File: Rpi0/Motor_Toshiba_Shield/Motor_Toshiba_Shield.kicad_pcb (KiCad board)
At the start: 2 copper layers, 29.8 x 64.8 mm, 34 parts, among them J1 Screw_Terminal_01x02, J10 Conn_01x04_Female, J11 Conn_01x04_Female, J2 Conn_02x01, J3 Screw_Terminal_01x02, J4 Screw_Terminal_01x02, J5 Screw_Terminal_01x02, J6 Screw_Terminal_01x02, J7 Conn_02x01, J8 Conn_01x04_Female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

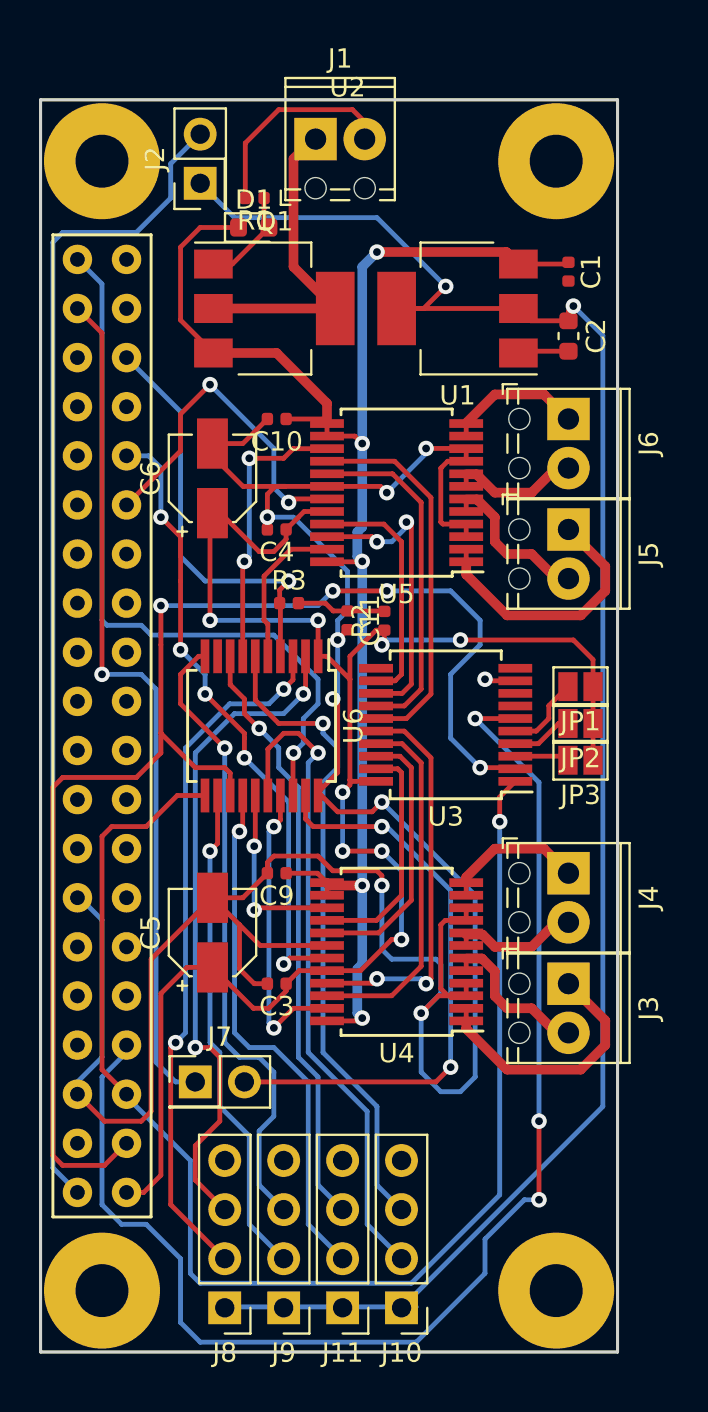
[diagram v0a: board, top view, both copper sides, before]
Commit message: Replaced pic16lf1509 and MCP by pic16f1777
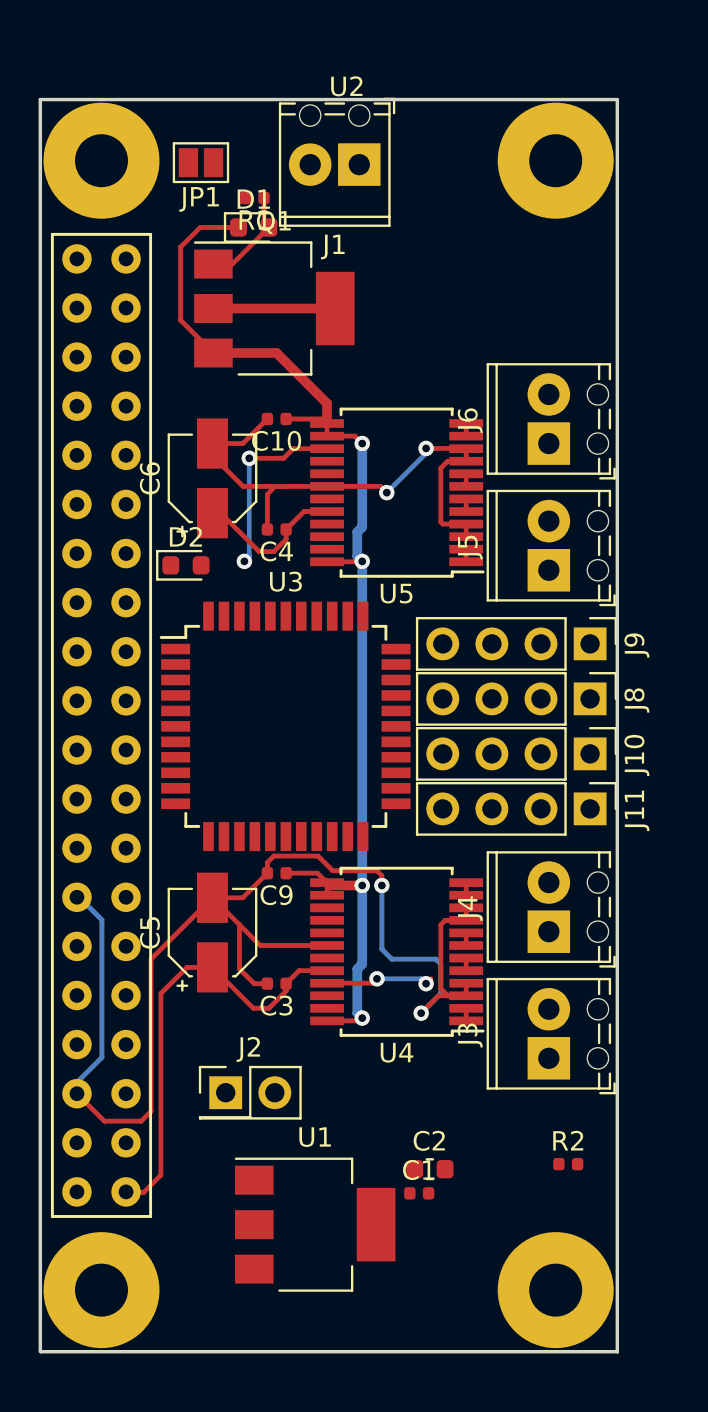
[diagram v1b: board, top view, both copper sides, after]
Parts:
- removed C11: 1uF, Capacitor_SMD:C_0402_1005Metric
- removed J7: Conn_02x01, Connector_PinHeader_2.54mm:PinHeader_2x01_P2.54mm_Vertical
- removed JP2, JP3: SolderJumper_2_Open, Jumper:SolderJumper-2_P1.3mm_Open_Pad1.0x1.5mm
- removed R3: 470, Resistor_SMD:R_0402_1005Metric
- removed U6: PIC16F1509-ISS, Package_SO:SSOP-20_5.3x7.2mm_P0.65mm
- added D2: LED, LED_SMD:LED_0603_1608Metric, F.Cu at (114.8, 86.3)
- R2: value 10k -> 50
- U3: value MCP23008_SSOP -> PIC16F1777-TQFP; footprint Package_SO:SSOP-20_5.3x7.2mm_P0.65mm -> Package_QFP:TQFP-44_10x10mm_P0.8mm
- moved C1 48.3 mm to (126.9, 118.8), turned to 0 degrees
- moved U1 48.0 mm to (121.5, 120.4), turned to 0 degrees
- moved J2 47.1 mm to (116.9, 113.6), turned to 0 degrees
- moved C2 43.7 mm to (127.4, 117.5), turned to 0 degrees
- moved J9 37.8 mm to (135.7, 90.4), turned to 270 degrees
- moved J8 36.7 mm to (135.7, 93.2), turned to 270 degrees
- moved JP1 33.5 mm to (115.6, 65.5)
- moved J10 30.3 mm to (135.7, 96.1), turned to 270 degrees
- moved R2 29.7 mm to (134.6, 117.3), turned to 0 degrees
- moved J11 28.8 mm to (135.7, 98.9), turned to 270 degrees
- moved U3 8.27 mm to (120.0, 94.6), turned to 0 degrees
- moved J3 3.99 mm to (133.6, 111.8), turned to 90 degrees
- moved J4 3.19 mm to (133.6, 105.3), turned to 90 degrees
- moved J1 2.62 mm to (123.8, 65.6), turned to 180 degrees
- moved J5 2.34 mm to (133.6, 86.6), turned to 90 degrees
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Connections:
- JP1 pad 1: +3V3 -> Net-(JP1-Pad1)
- JP1 pad 2: Net-(JP1-Pad2) -> ICSP_DAT
- R2 pad 1: +3V3 -> Net-(R2-Pad1)
- U2 pad 29: EN1 -> Net-(U2-Pad29)
- U2 pad 31: EN2 -> Net-(U2-Pad31)
- U2 pad 7: RES -> Net-(U2-Pad7)
- U3 pad 1: SCL -> Net-(U3-Pad1)
- U3 pad 10: (no net) -> A4
- U3 pad 11: (no net) -> B4
- U3 pad 12: INA1 -> Net-(U3-Pad12)
- U3 pad 13: INA2 -> Net-(U3-Pad13)
- U3 pad 14: INB1 -> Net-(R2-Pad1)
- U3 pad 15: INB2 -> Net-(U3-Pad15)
- U3 pad 16: INA3 -> ICSP_CLK
- U3 pad 17: INA4 -> Net-(JP1-Pad1)
- U3 pad 18: INB3 -> MCLR
- U3 pad 19: INB4 -> PWM4
- U3 pad 2: SDA -> INA3
- U3 pad 20: +3V3 -> PWM1
- U3 pad 3: Net-(JP3-Pad2) -> INA4
- U3 pad 4: Net-(JP2-Pad2) -> INB3
- U3 pad 5: Net-(JP1-Pad2) -> INB4
- U3 pad 6: RES -> BAT-
- U3 pad 7: (no net) -> +3V3
- U3 pad 8: Net-(U3-Pad8) -> A3
- U3 pad 9: BAT- -> B3
- U4 pad 11: Net-(J4-Pad1) -> Net-(J4-Pad2)
- U4 pad 12: Net-(J4-Pad1) -> Net-(J4-Pad2)
- U4 pad 7: Net-(J4-Pad2) -> Net-(J4-Pad1)
- U4 pad 8: Net-(J4-Pad2) -> Net-(J4-Pad1)
- U5 pad 11: Net-(J6-Pad1) -> Net-(J6-Pad2)
- U5 pad 12: Net-(J6-Pad1) -> Net-(J6-Pad2)
- U5 pad 7: Net-(J6-Pad2) -> Net-(J6-Pad1)
- U5 pad 8: Net-(J6-Pad2) -> Net-(J6-Pad1)
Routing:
- net +5V: track 93.8 -> 0.00 mm, vias 2 -> 0
- net SDA: track 71.3 -> 0.00 mm, vias 4 -> 0
- net SCL: track 70.5 -> 0.13 mm, vias 1 -> 0
- net RES: track 68.7 -> 0.00 mm, vias 3 -> 0
- net BAT-: track 159.9 -> 99.1 mm, vias 9 -> 4
- net Net-(J2-Pad2): track 61.3 -> 0.64 mm
- net +3V3: track 88.7 -> 30.5 mm, vias 8 -> 0
- net ICSP_DAT: track 44.3 -> 0.00 mm, vias 1 -> 0
- net ICSP_CLK: track 38.2 -> 0.00 mm, vias 1 -> 0
- net A1: track 36.1 -> 0.00 mm, vias 2 -> 0
- net B1: track 34.6 -> 0.00 mm, vias 2 -> 0
- net A3: track 34.1 -> 0.00 mm, vias 1 -> 0
- net B3: track 33.7 -> 0.00 mm, vias 1 -> 0
- net EN2: track 32.9 -> 0.00 mm, vias 5 -> 0
- net B2: track 32.8 -> 0.00 mm, vias 1 -> 0
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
